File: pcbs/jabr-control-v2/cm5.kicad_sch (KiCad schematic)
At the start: 17 parts, among them J201 JST-SH-4-Vertical, SW202 TS20-42-25-WT-160-SMT-TR, U201 NX3DV221TKX

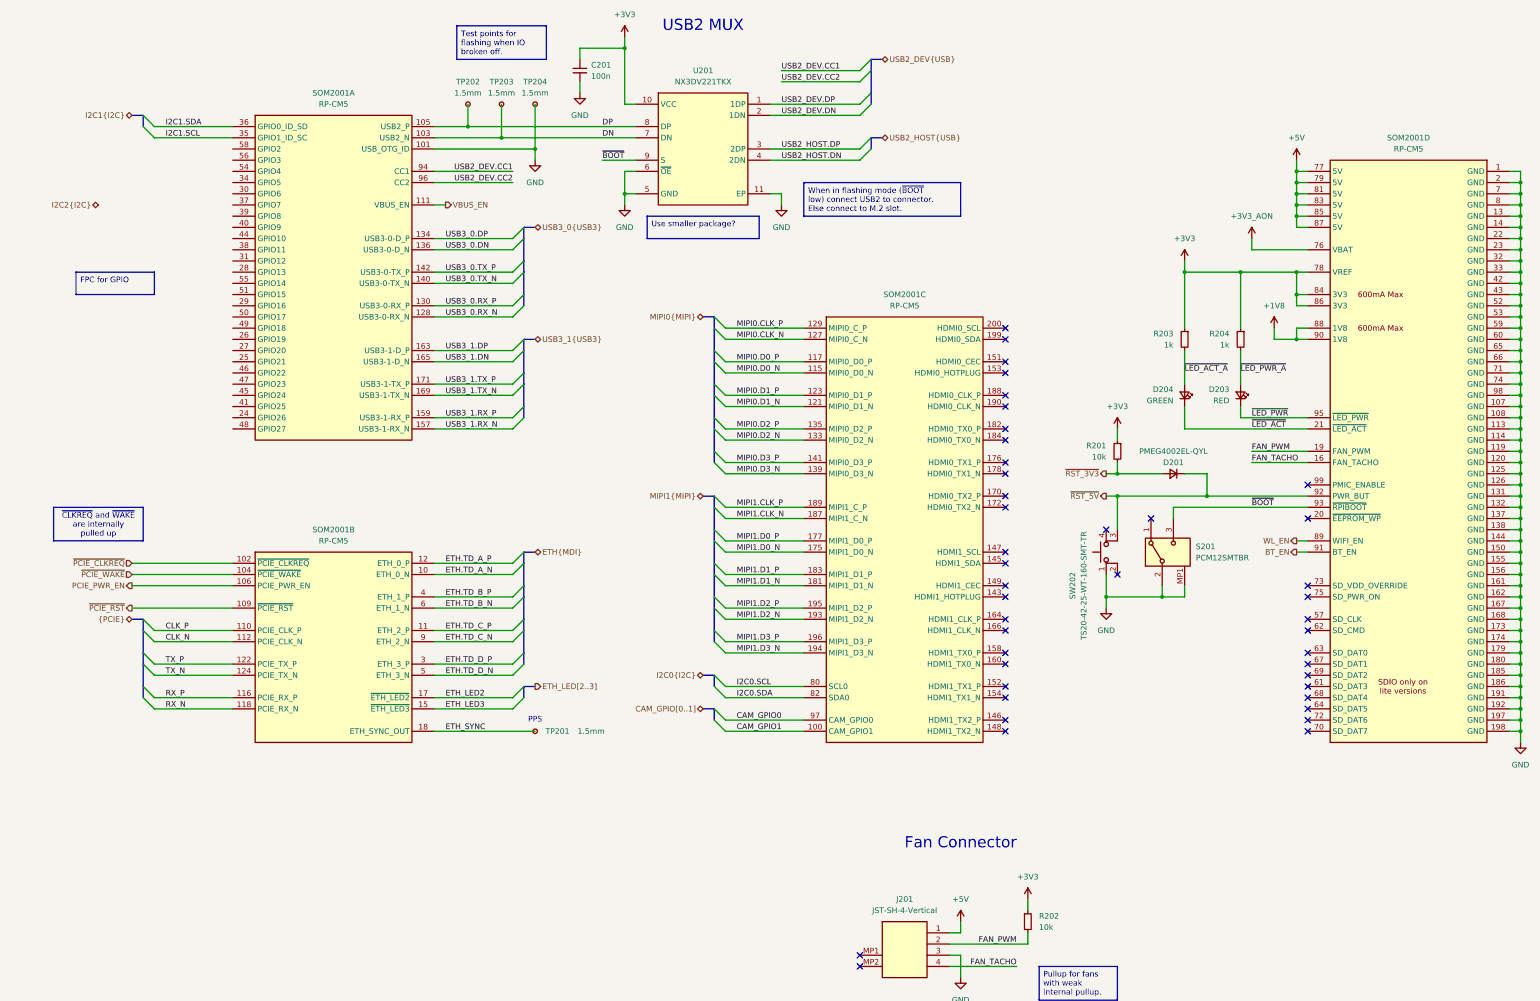
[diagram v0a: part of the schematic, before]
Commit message: PCI11010C Schematic sheet mostly done
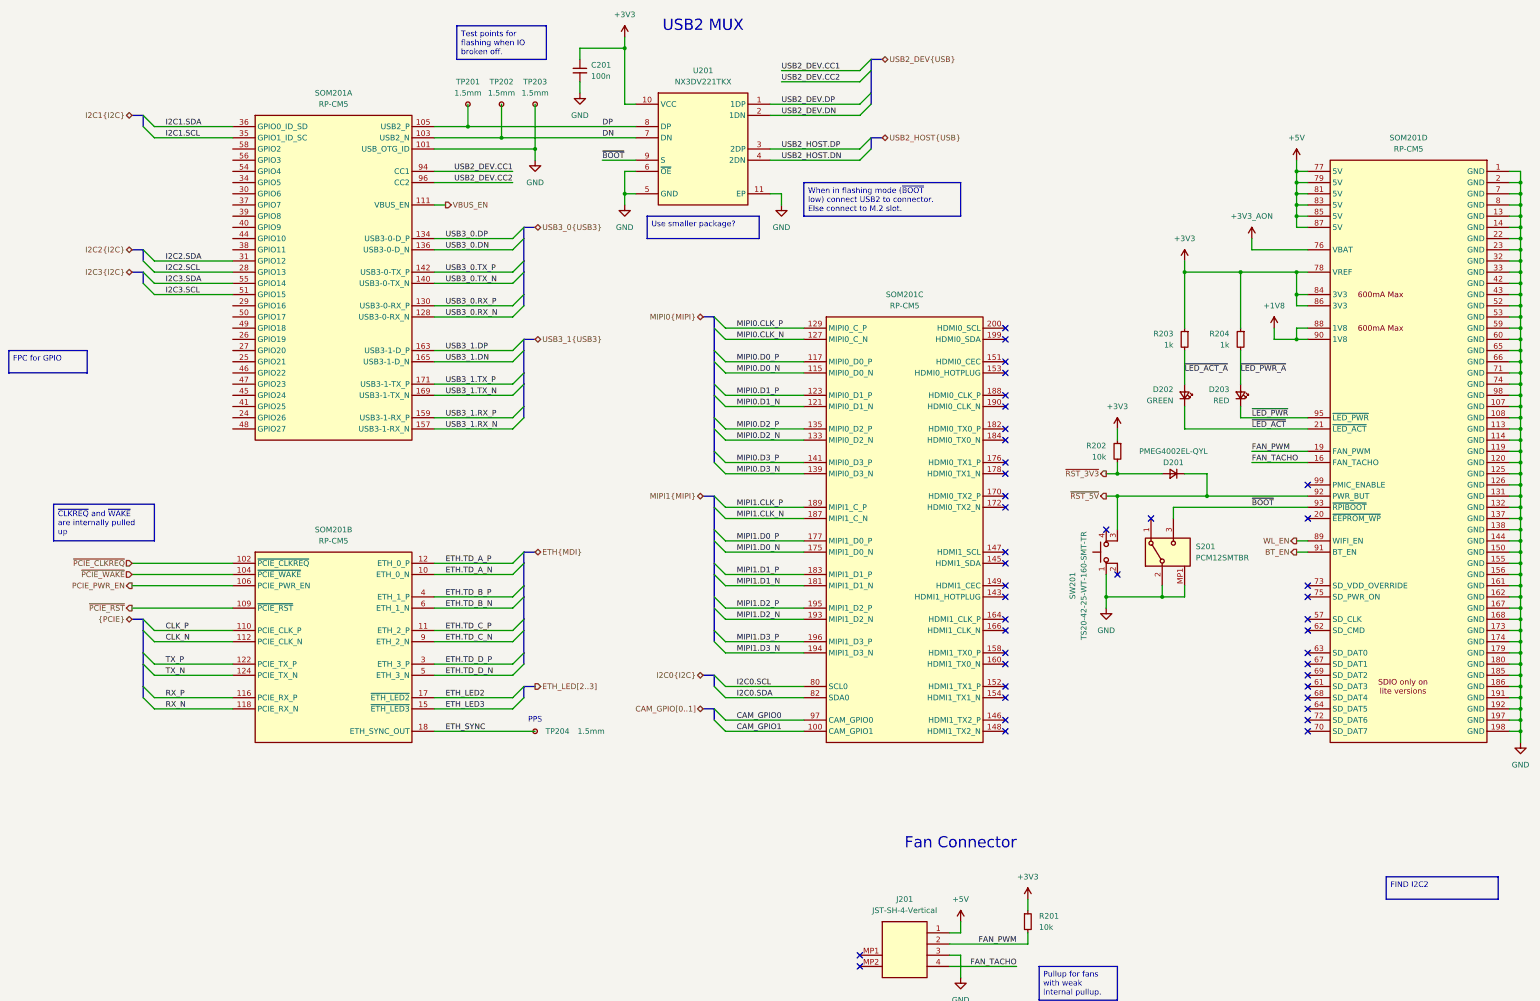
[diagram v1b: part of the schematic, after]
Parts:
- renumbered D204 to D202, R202 to R201, R201 to R202, SOM2001 to SOM201, SW202 to SW201, TP202 to TP201, TP203 to TP202, TP204 to TP203, TP201 to TP204
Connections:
- net I2C2.SCL: now reaches SOM201.28 (GPIO13)
- net I2C2.SDA: now reaches SOM201.31 (GPIO12)
- net I2C3.SCL: now reaches SOM201.51 (GPIO15)
- net I2C3.SDA: now reaches SOM201.55 (GPIO14)

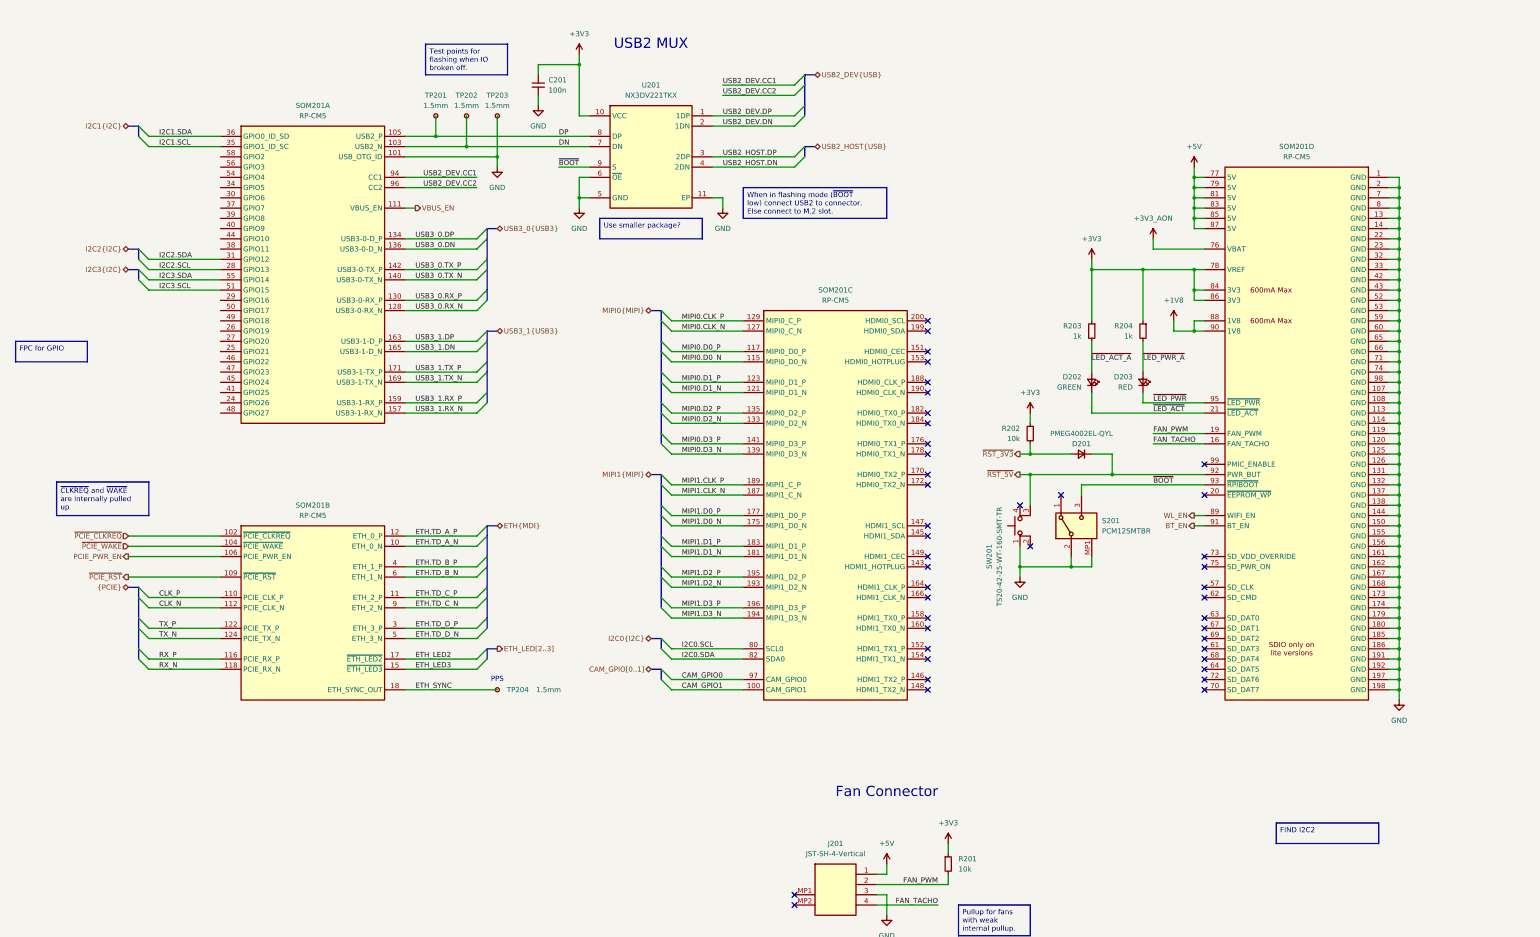
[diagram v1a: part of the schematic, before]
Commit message: Moved M.2 buffers to new sheet
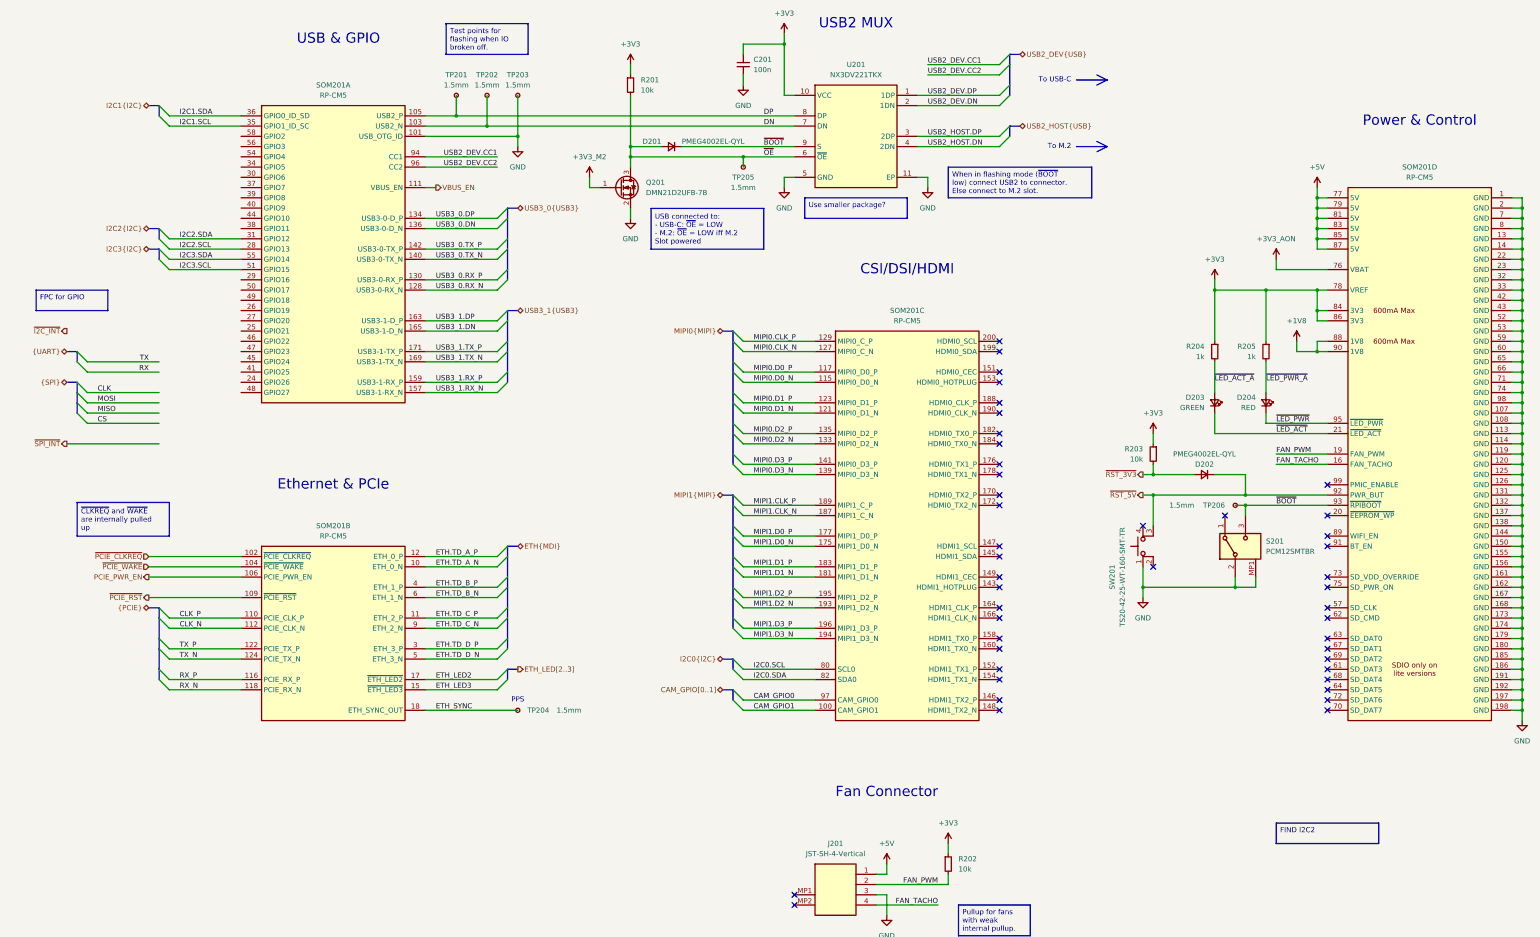
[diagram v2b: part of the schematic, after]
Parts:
- added D201: PMEG4002EL-QYL, project_footprints:PMEG4002EL-QYL, symbol DIODE:PMEG4002EL-QYL
- added Q201: DMN21D2UFB-7B, project_footprints:DMN21D2UFB7B, symbol MOSFET:DMN21D2UFB-7B
- added R201: 10k, project_footprints:R_0402, symbol DEV:R_SMALL
- added TP205, TP206: 1.5mm, project_footprints:TestPoint_Pad_D1.5mm, symbol Connector:TestPoint_Small
- renumbered D201 to D202, D202 to D203, D203 to D204, R201 to R202, R202 to R203, R203 to R204, R204 to R205
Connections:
- net +3V3: now also R201.1
- net GND: now also Q201.2 (S); no longer U201.6 (~{OE})
- net ~{BOOT}: now also D201.1 (K), TP206.1
- net BT_EN: no longer names the net of SOM201.91 (BT_EN)
- net WL_EN: no longer names the net of SOM201.89 (WIFI_EN)
- new net +3V3_M2: Q201.1 (G)
- new net ~{OE}: D201.2 (A), Q201.3 (D), R201.2, TP205.1, U201.6 (~{OE})
- no-connect marks 43 -> 45
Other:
- note added: "CSI/DSI/HDMI"
- note added: "Ethernet & PCIe"
- note added: "Power & Control"
- note added: "To M.2"
- note added: "To USB-C"
- note added: "USB & GPIO"
- moved on the sheet: C201, D202, D203, D204, R203, R204, R205, S201, SOM201A, SOM201B, SOM201C, SOM201D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
